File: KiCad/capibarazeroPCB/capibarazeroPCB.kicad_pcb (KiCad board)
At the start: 2 copper layers, 95 x 89 mm, 21 parts, among them J1 Conn_01x15, J2 Conn_01x15, J3 PINHD_1x6_Male, J4 PINHD_1x4_Male, J5 PINHD_1x8_Male, J6 PINHD_1x3_Male, SW1 SW_Push, SW1_R1 SW_Push, SW2_L1 SW_Push, SW3_M1 SW_Push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

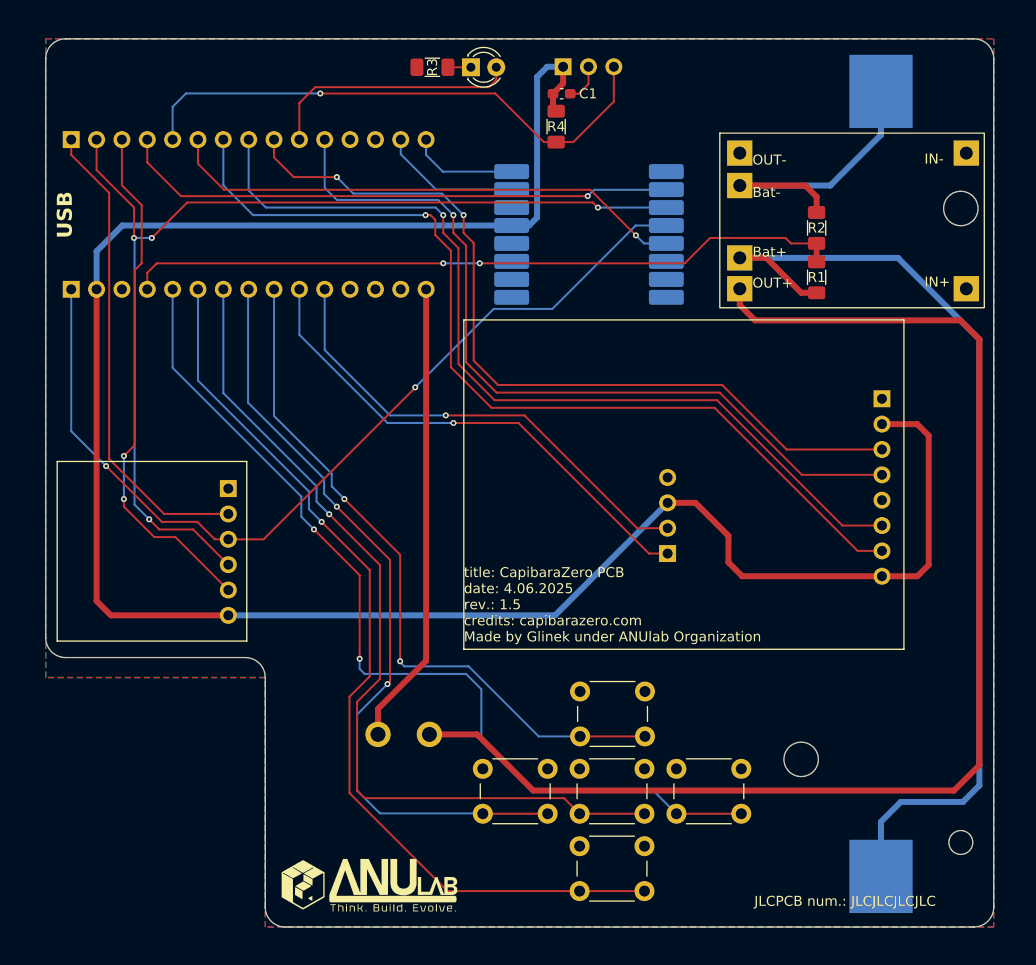
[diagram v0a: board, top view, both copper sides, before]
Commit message: pcb update to rev2 - 08.07.2025
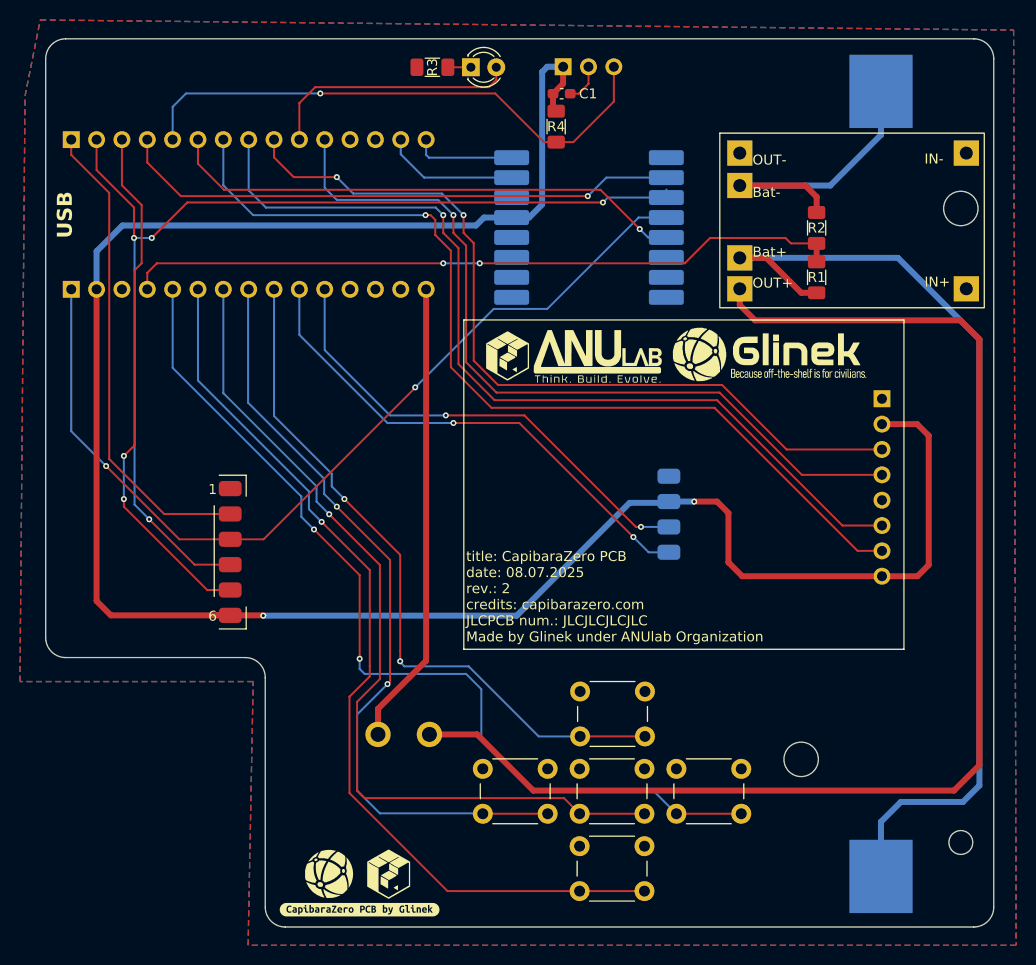
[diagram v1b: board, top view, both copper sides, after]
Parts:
- added kibuzzard-686CF35A: G***, kibuzzard-686CF35A, F.Cu at (124.8, 149.8)
- J3: footprint Connector_PinHeader_2.54mm:PinHeader_1x06_P2.54mm_Vertical -> ExtFootprints:smd_connectorGeneric_1x6-2.54mm
- J4: footprint Connector_PinHeader_2.54mm:PinHeader_1x04_P2.54mm_Vertical -> ExtFootprints:smd_connecorGeneric_1x4-2.54mm
- moved J4 9.76 mm to (162.7, 120.8)
- moved J3 4.97 mm to (110.0, 102.9)
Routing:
- net +3.3V: track 214.5 -> 215.4 mm, vias 0 -> 2
- net D1: track 10.8 -> 10.2 mm
- net A6: track 50.5 -> 50.6 mm, vias 1 -> 2
- net A7: track 47.8 -> 47.9 mm, vias 1 -> 2
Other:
- board text added: "Soldering order: 1) Resistors and capacitors 2) LoRa 3) Buttons* 4) RFID 5) Micro SD card reader 6) BMS 7) Display** 8) IR stuff 9) Arduino 10) Battery holder Important! * Make sure to cut some legs to assure that NFC chip lays flat ** Solder pins flat with the bottom of the PCB, other wise 18650 won't fit"
- board text added: "title: CapibaraZero PCB date: 08.07.2025 rev.: 2 credits: capibarazero.com JLCPCB num.: JLCJLCJLCJLC Made by Glinek under ANUlab Organization"
- board text removed: "JLCPCB num.: JLCJLCJLCJLC"
- board text removed: "title: CapibaraZero PCB date: 4.06.2025 rev.: 1.5 credits: capibarazero.com Made by Glinek under ANUlab Organization"
